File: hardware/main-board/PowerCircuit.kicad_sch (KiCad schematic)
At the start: 21 parts, among them U1 XTPS55285VALR

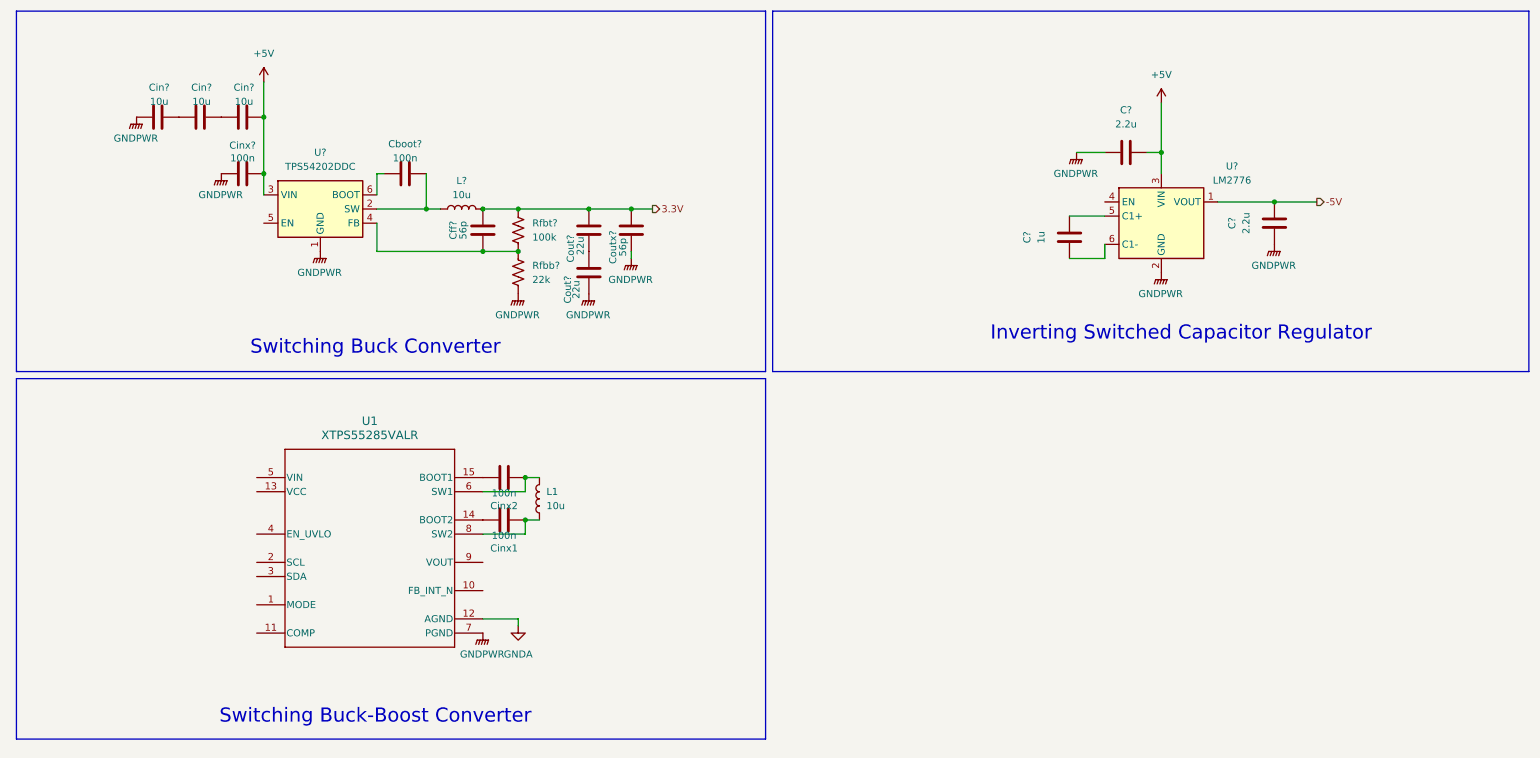
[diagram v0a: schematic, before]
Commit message: Updated Footprints and Controls
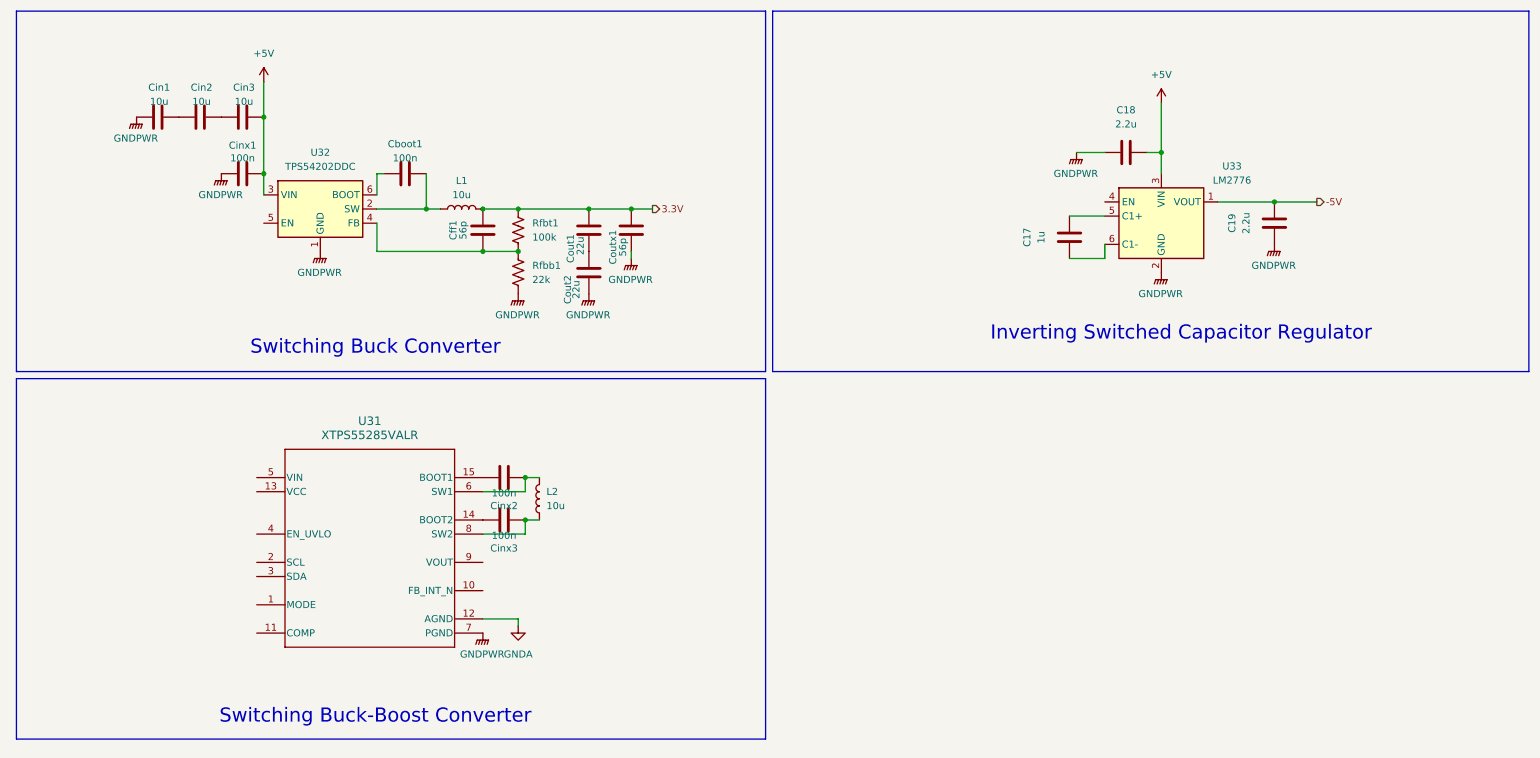
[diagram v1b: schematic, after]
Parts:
- U31: renamed from U1; footprint VAL0015A-MFG -> (none)
- gave numbers to parts that had none: 17
- renumbered Cinx1 to Cinx3, L1 to L2

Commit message: Designated majority of footprints
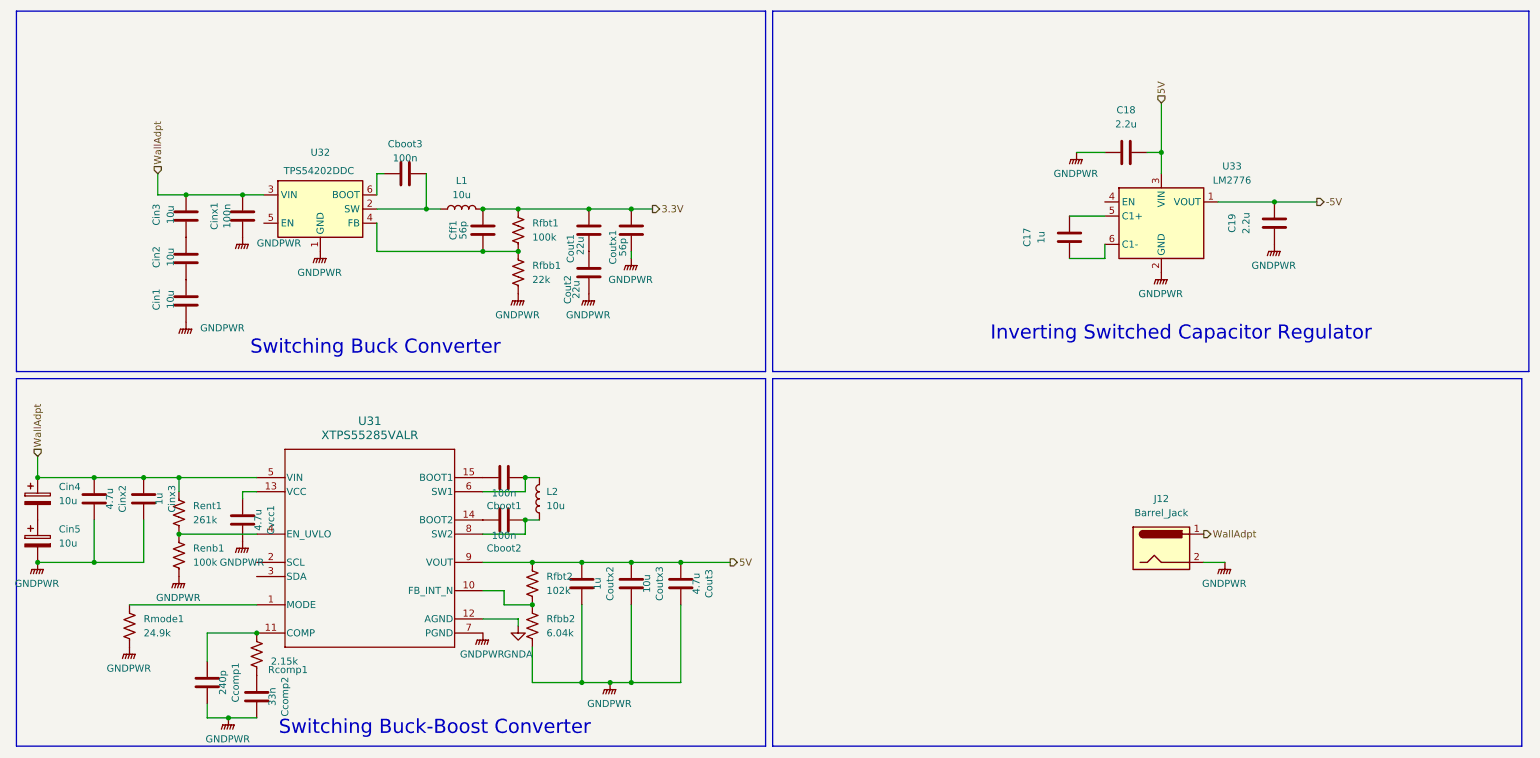
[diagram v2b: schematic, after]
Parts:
- added Ccomp1: 240p, Capacitor_SMD:C_0402_1005Metric_Pad0.74x0.62mm_HandSolder, symbol Device:C
- added Ccomp2: 33n, Capacitor_SMD:C_0402_1005Metric_Pad0.74x0.62mm_HandSolder, symbol Device:C
- added Cin4, Cin5: 10u, SeniorDesignFP:CAP_EEFK_C_PAN, symbol Device:C_Polarized
- added Cinx2: 4.7u, Capacitor_SMD:C_1210_3225Metric_Pad1.33x2.70mm_HandSolder, symbol Device:C
- added Cinx3: 1u, Capacitor_SMD:C_0402_1005Metric_Pad0.74x0.62mm_HandSolder, symbol Device:C
- added Cout3: 4.7u, Capacitor_SMD:C_1206_3216Metric_Pad1.33x1.80mm_HandSolder, symbol Device:C
- added Coutx2: 1u, Capacitor_SMD:C_0201_0603Metric_Pad0.64x0.40mm_HandSolder, symbol Device:C
- added Coutx3: 10u, Capacitor_SMD:C_1210_3225Metric_Pad1.33x2.70mm_HandSolder, symbol Device:C
- added Cvcc1: 4.7u, Capacitor_SMD:C_0201_0603Metric_Pad0.64x0.40mm_HandSolder, symbol Device:C
- added J12: Barrel_Jack, Connector_BarrelJack:BarrelJack_CUI_PJ-063AH_Horizontal, symbol Connector:Barrel_Jack
- added Rcomp1: 2.15k, Resistor_SMD:R_0402_1005Metric_Pad0.72x0.64mm_HandSolder, symbol Device:R_US
- added Renb1: 100k, Resistor_SMD:R_0402_1005Metric_Pad0.72x0.64mm_HandSolder, symbol Device:R_US
- added Rent1: 261k, Resistor_SMD:R_0402_1005Metric_Pad0.72x0.64mm_HandSolder, symbol Device:R_US
- added Rfbb2: 6.04k, Resistor_SMD:R_0402_1005Metric_Pad0.72x0.64mm_HandSolder, symbol Device:R_US
- added Rfbt2: 102k, Resistor_SMD:R_0402_1005Metric_Pad0.72x0.64mm_HandSolder, symbol Device:R_US
- added Rmode1: 24.9k, Resistor_SMD:R_0402_1005Metric_Pad0.72x0.64mm_HandSolder, symbol Device:R_US
- C17, C18, C19: footprint (none) -> Capacitor_SMD:C_0603_1608Metric_Pad1.08x0.95mm_HandSolder
- Cboot1: renamed from Cinx2; footprint (none) -> Capacitor_SMD:C_0402_1005Metric_Pad0.74x0.62mm_HandSolder
- Cboot2: renamed from Cinx3; footprint (none) -> Capacitor_SMD:C_0402_1005Metric_Pad0.74x0.62mm_HandSolder
- Cboot3: renamed from Cboot1; footprint (none) -> Capacitor_SMD:C_0402_1005Metric_Pad0.74x0.62mm_HandSolder
- Cff1: footprint (none) -> Capacitor_SMD:C_0201_0603Metric_Pad0.64x0.40mm_HandSolder
- Cin1, Cin2, Cin3: footprint (none) -> Capacitor_SMD:C_1210_3225Metric_Pad1.33x2.70mm_HandSolder
- Cinx1: footprint (none) -> Capacitor_SMD:C_0402_1005Metric_Pad0.74x0.62mm_HandSolder
- Cout1, Cout2: footprint (none) -> Capacitor_SMD:C_0805_2012Metric_Pad1.18x1.45mm_HandSolder
- Coutx1, Rfbt1: footprint (none) -> Resistor_SMD:R_0402_1005Metric_Pad0.72x0.64mm_HandSolder
- L1: footprint (none) -> Inductor_SMD:L_Bourns-SRU1028_10.0x10.0mm; Comment (none) -> SRU 1048 but package is same
- L2: footprint (none) -> Inductor_SMD:L_Bourns_SDR0604
- Rfbb1: footprint (none) -> Resistor_SMD:R_0201_0603Metric_Pad0.64x0.40mm_HandSolder
- U31: footprint (none) -> SeniorDesignFP:TPS55285
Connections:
- net GNDPWR: now also Ccomp1.2, Ccomp2.2, Cin5.2, Cinx2.2, Cinx3.2, Cout3.2, Coutx2.2, Coutx3.2, Cvcc1.2, J12.2, Renb1.2, Rfbb2.2, Rmode1.2
- net at U31.1 (MODE): now also Rmode1.1
- net at U31.10 (FB_INT_N): now also Rfbb2.1, Rfbt2.2
- net at U31.11 (COMP): now also Ccomp1.1, Rcomp1.1
- net at U31.13 (VCC): now also Cvcc1.1
- net at U31.4 (EN_UVLO): now also Renb1.1, Rent1.2
- net WallAdpt: now reaches U31.5 (VIN)
- net WallAdpt: now also Cin3.2, Cinx1.2, U32.3 (VIN), Cin4.1, Cinx2.1, Cinx3.1, J12.1, Rent1.1
- net 5V: now reaches U31.9 (VOUT)
- net 5V: now also C18.2, U33.3 (VIN), Cout3.1, Coutx2.1, Coutx3.1, Rfbt2.1
- removed net +5V: C18.2, Cin3.2, Cinx1.2, U32.3 (VIN), U33.3 (VIN)
- new net: Ccomp2.1, Rcomp1.2
- new net: Cin4.2, Cin5.1
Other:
- moved on the sheet: Cin1, Cin2, Cin3, Cinx1

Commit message: designed Power PCB section layout
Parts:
- renumbered Cboot3 to Cboot1, Cboot1 to Cboot2, Cboot2 to Cboot3, Cin4 to Cin1, Cin5 to Cin2, Cin2 to Cin4, Cin1 to Cin5, Cinx2 to Cinx1, Cinx3 to Cinx2, Cinx1 to Cinx3, Coutx2 to Coutx1, Coutx1 to Coutx2, J12 to J9
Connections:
- net GNDA renamed GND
- no-connect marks 0 -> 4

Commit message: added ground conn and fixed switches
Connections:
- net GNDPWR is gone; now on net GND: C18.1, C19.1, Ccomp1.2, Ccomp2.2, Cin2.2, Cin5.1, Cinx1.2, Cinx2.2, Cinx3.1, Cout2.1, Cout3.2, Coutx1.2, Coutx2.1, Coutx3.2, Cvcc1.2, J9.2, Renb1.2, Rfbb1.2, Rfbb2.2, Rmode1.2, U31.7 (PGND), U32.1 (GND), U33.2 (GND)
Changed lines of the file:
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@@
 	(wire
 		(pts
+			(xy 171.45 107.95) (xy 179.07 107.95)
+		)
+		(stroke
+			(width 0)
+			(type default)
+		)
+	)
+	(wire
+		(pts
 			(xy 96.52 116.84) (xy 100.33 116.84)
 		)
@@
 	(symbol
 		(lib_id "power:GNDPWR")
+		(at 179.07 107.95 0)
+		(unit 1)
+		(exclude_from_sim no)
+		(in_bom yes)
+		(on_board yes)
+		(dnp no)
+		(fields_autoplaced yes)
+		(property "Reference" "#PWR030"
+			(at 179.07 113.03 0)
+			(effects
+				(font
+					(size 1.27 1.27)
+				)
+				(hide yes)
+			)
+		)
+		(property "Value" "GNDPWR"
+			(at 178.943 111.76 0)
+			(effects
+				(font
+					(size 1.27 1.27)
+				)
+			)
+		)
+		(property "Footprint" ""
+			(at 179.07 109.22 0)
+			(effects
+				(font
+					(size 1.27 1.27)
+				)
+				(hide yes)
+			)
+		)
+		(property "Datasheet" ""
+			(at 179.07 109.22 0)
+			(effects
+				(font
+					(size 1.27 1.27)
+				)
+				(hide yes)
+			)
+		)
+		(property "Description" "Power symbol creates a global label with name \"GNDPWR\" , global ground"
+			(at 179.07 107.95 0)
+			(effects
+				(font
+					(size 1.27 1.27)
+				)
+				(hide yes)
+			)
+		)
+		(pin "1"
+		)
+		(instances
+			(project "MainBoard"
+				(path "/5dd933ff-bc57-4741-8957-85d8c6e75130/534f316e-b737-411c-8d6f-20e6ab703659"
+					(reference "#PWR030")
+					(unit 1)
+				)
+			)
+		)
+	)
+	(symbol
+		(lib_id "power:GNDPWR")
 		(at 67.31 55.88 0)
 		(unit 1)
@@
 					(unit 1)
 				)
+			)
+		)
+	)
+	(symbol
+		(lib_id "power:GND")
+		(at 171.45 107.95 0)
+		(unit 1)
+		(exclude_from_sim no)
+		(in_bom yes)
+		(on_board yes)
+		(dnp no)
+		(fields_autoplaced yes)
+		(property "Reference" "#PWR035"
+			(at 171.45 114.3 0)
+			(effects
+				(font
+					(size 1.27 1.27)
+				)
+				(hide yes)
+			)
+		)
+		(property "Value" "GND"
+			(at 171.45 113.03 0)
+			(effects
+				(font
+					(size 1.27 1.27)
+				)
+			)
+		)
+		(property "Footprint" ""
+			(at 171.45 107.95 0)
+			(effects
+				(font
+					(size 1.27 1.27)
+				)
+				(hide yes)
+			)
+		)
+		(property "Datasheet" ""
+			(at 171.45 107.95 0)
+			(effects
+				(font
+					(size 1.27 1.27)
+				)
+				(hide yes)
+			)
+		)
+		(property "Description" "Power symbol creates a global label with name \"GND\" , ground"
+			(at 171.45 107.95 0)
+			(effects
+				(font
+					(size 1.27 1.27)
+				)
+				(hide yes)
+			)
+		)
+		(pin "1"
+		)
+		(instances
+			(project "MainBoard"
+				(path "/5dd933ff-bc57-4741-8957-85d8c6e75130/534f316e-b737-411c-8d6f-20e6ab703659"
+					(reference "#PWR035")
+					(unit 1)
+				)

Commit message: feat: ERC + DRC fixes
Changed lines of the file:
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@@
 	)
 	(junction
-		(at 226.06 111.76)
-		(diameter 0)
-		(color 0 0 0 0)
-	)
-	(junction
 		(at 55.88 124.46)
 		(diameter 0)
@@
 					(unit 1)
 				)
-			)
-		)
-	)
-	(symbol
-		(lib_id "power:PWR_FLAG")
-		(at 226.06 111.76 180)
-		(unit 1)
-		(exclude_from_sim no)
-		(in_bom yes)
-		(on_board yes)
-		(dnp no)
-		(fields_autoplaced yes)
-		(property "Reference" "#FLG05"
-			(at 226.06 113.665 0)
-			(effects
-				(font
-					(size 1.27 1.27)
-				)
-				(hide yes)
-			)
-		)
-		(property "Value" "PWR_FLAG"
-			(at 226.06 116.84 0)
-			(effects
-				(font
-					(size 1.27 1.27)
-				)
-			)
-		)
-		(property "Footprint" ""
-			(at 226.06 111.76 0)
-			(effects
-				(font
-					(size 1.27 1.27)
-				)
-				(hide yes)
-			)
-		)
-		(property "Datasheet" "~"
-			(at 226.06 111.76 0)
-			(effects
-				(font
-					(size 1.27 1.27)
-				)
-				(hide yes)
-			)
-		)
-		(property "Description" "Special symbol for telling ERC where power comes from"
-			(at 226.06 111.76 0)
-			(effects
-				(font
-					(size 1.27 1.27)
-				)
-				(hide yes)
-			)
-		)
-		(pin "1"
-		)
-		(instances
-			(project ""
-				(path "/5dd933ff-bc57-4741-8957-85d8c6e75130/534f316e-b737-411c-8d6f-20e6ab703659"
-					(reference "#FLG05")
-					(unit 1)
-				)

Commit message: feat: Part nos plus some micro fixup
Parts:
- C17: value 1u -> 1µF; DKPN (none) -> C0603C105K4RACTU
- Cboot1, Cboot2, Cboot3, Cinx3: value 100n -> 100nF
- Cin1, Cin2, Cin3, Cin4, Cin5, Coutx3: value 10u -> 10µF
- Cinx2, Coutx1: value 1u -> 1µF
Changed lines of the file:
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@@
 			)
 		)
-		(property "Value" "10u"
+		(property "Value" "10µF"
 			(at 20.32 100.7109 0)
 			(effects
@@
 			)
 		)
-		(property "Value" "1u"
+		(property "Value" "1µF"
 			(at 38.354 100.33 90)
 			(effects
@@
 			)
 		)
-		(property "Value" "10u"
+		(property "Value" "10µF"
 			(at 20.32 108.3309 0)
 			(effects
@@
 			)
 		)
-		(property "Value" "10u"
+		(property "Value" "10µF"
 			(at 40.386 49.276 90)
 			(effects
@@
 			)
 		)
-		(property "Value" "100n"
+		(property "Value" "100nF"
 			(at 82.55 39.116 90)
 			(effects
@@
 			)
 		)
-		(property "Value" "100n"
+		(property "Value" "100nF"
 			(at 100.33 99.314 90)
 			(effects
@@
 			)
 		)
-		(property "Value" "10u"
+		(property "Value" "10µF"
 			(at 125.984 115.57 90)
 			(effects
@@
 			)
 		)
-		(property "Value" "1u"
+		(property "Value" "1µF"
 			(at 117.094 115.57 90)
 			(effects
@@
 			)
 		)
-		(property "Value" "1u"
+		(property "Value" "1µF"
 			(at 196.85 53.34 90)
 			(effects
@@
 			)
 		)
+		(property "DKPN" "C0603C105K4RACTU"
+			(at 201.93 53.34 90)
+			(effects
+				(font
+					(size 1.27 1.27)
+				)
+				(hide yes)
+			)
+		)
 		(pin "2"
 		)
@@
 			)
 		)
-		(property "Value" "10u"
+		(property "Value" "10µF"
 			(at 40.386 64.516 90)
 			(effects
@@
 			)
 		)
-		(property "Value" "100n"
+		(property "Value" "100nF"
 			(at 50.546 49.53 90)
 			(effects
@@
 			)
 		)
-		(property "Value" "100n"
+		(property "Value" "100nF"
 			(at 100.33 106.934 90)
 			(effects
@@
 			)
 		)
-		(property "Value" "10u"
+		(property "Value" "10µF"
 			(at 40.386 56.896 90)
 			(effects
